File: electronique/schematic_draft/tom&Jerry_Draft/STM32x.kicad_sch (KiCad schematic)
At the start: 58 parts, among them IC4 STM32G431CBU3, J1 Conn_02x07_Odd_Even, SW1 SW_Push, SW2 SW_Push, SW3 SW_Push, SW4 SW_Push, Y1 16MHz

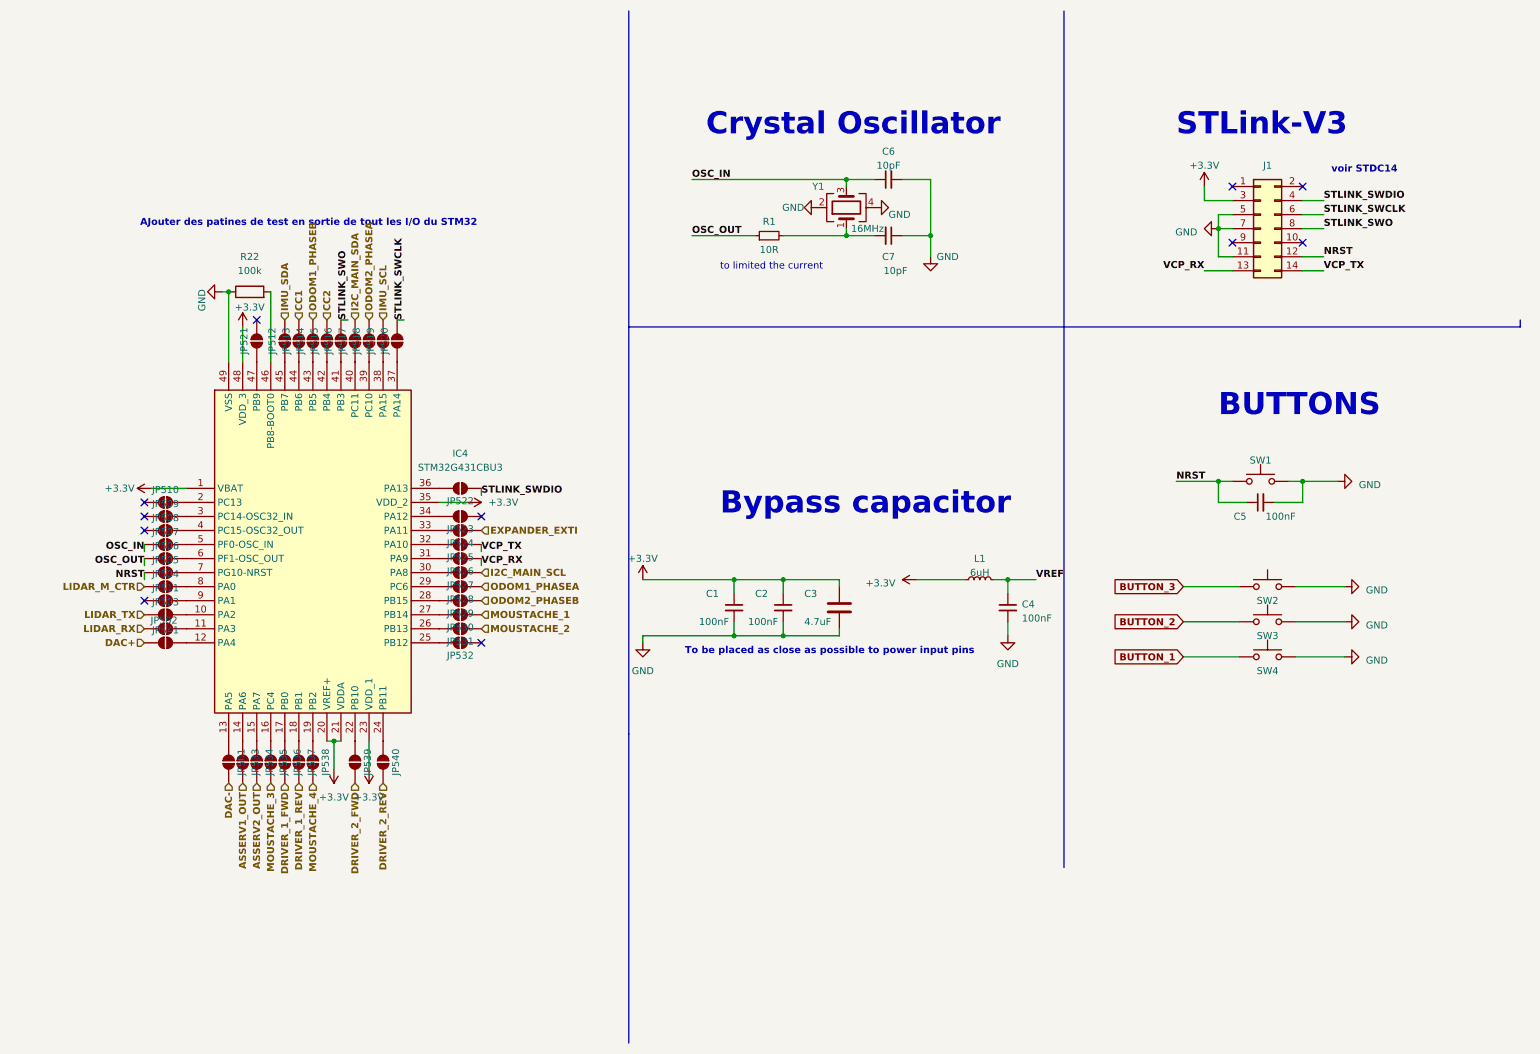
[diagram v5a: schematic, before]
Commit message: STM32 KiCAD V5 - 25.09.2024 - Ajout connecteurs TOF, ...
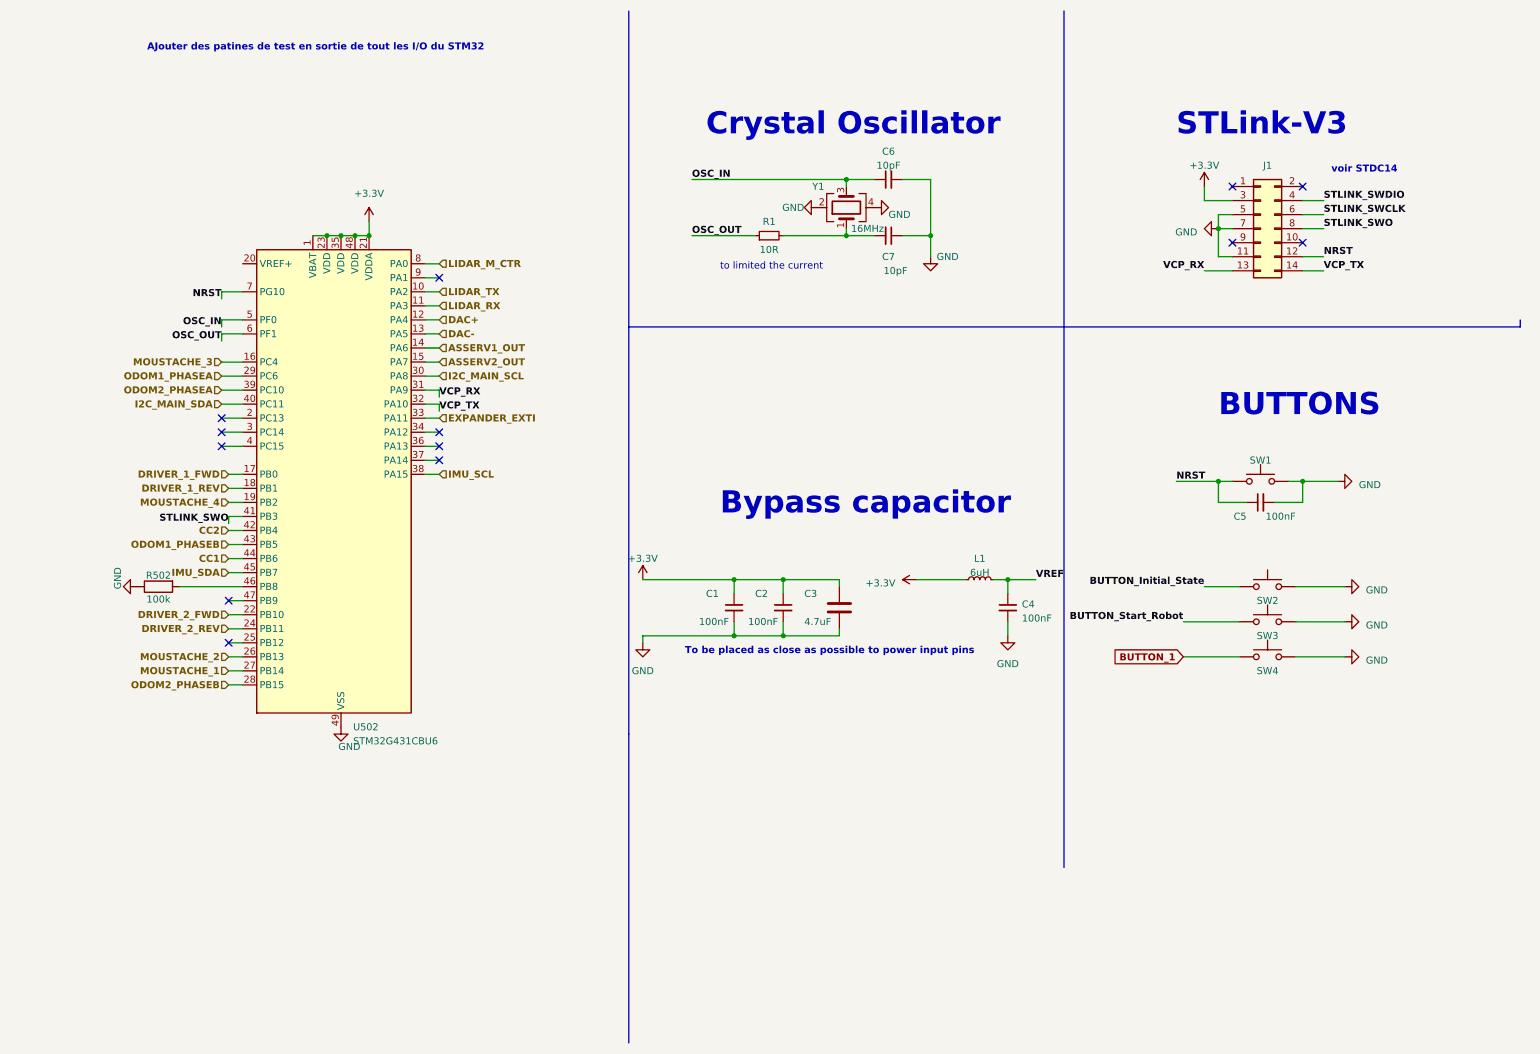
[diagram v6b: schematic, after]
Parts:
- removed IC4: STM32G431CBU3, QFN50P700X700X65-49N-D, symbol STM32G431CBU3:STM32G431CBU3
- removed JP501, JP502, JP503, JP504, JP505, JP506, JP507, JP508, JP509, JP510, JP511, JP512, JP513, JP514, JP515, JP516, JP517, JP518, JP519, JP520, JP521, JP522, JP523, JP524, JP525, JP526, JP527, JP528, JP529, JP530, JP531, JP532, JP533, JP534, JP535, JP536, JP537, JP538, JP539, JP540, JP541: SolderJumper_2_Open, symbol Jumper:SolderJumper_2_Open
- removed R22: 100k, symbol Device:R
- added R502: 100k, symbol Device:R
- added U502: STM32G431CBU6, Package_DFN_QFN:QFN-48-1EP_7x7mm_P0.5mm_EP5.6x5.6mm, symbol MCU_ST_STM32G4:STM32G431CBUx
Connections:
- net +3.3V: now also U502.1 (VBAT), U502.21 (VDDA), U502.23 (VDD), U502.35 (VDD), U502.48 (VDD)
- net ASSERV1_OUT: now also U502.14 (PA6)
- net ASSERV2_OUT: now also U502.15 (PA7)
- net CC1: now also U502.44 (PB6)
- net CC2: now also U502.42 (PB4)
- net DAC+: now also U502.12 (PA4)
- net DAC-: now also U502.13 (PA5)
- net DRIVER_1_FWD: now also U502.17 (PB0)
- net DRIVER_1_REV: now also U502.18 (PB1)
- net DRIVER_2_FWD: now also U502.22 (PB10)
- net DRIVER_2_REV: now also U502.24 (PB11)
- net EXPANDER_EXTI: now also U502.33 (PA11)
- net GND: now also R502.1, U502.49 (VSS)
- net I2C_MAIN_SCL: now also U502.30 (PA8)
- net I2C_MAIN_SDA: now also U502.40 (PC11)
- net IMU_SCL: now also U502.38 (PA15)
- net IMU_SDA: now also U502.45 (PB7)
- net LIDAR_M_CTR: now also U502.8 (PA0)
- net LIDAR_RX: now also U502.11 (PA3)
- net LIDAR_TX: now also U502.10 (PA2)
- net MOUSTACHE_1: now also U502.27 (PB14)
- net MOUSTACHE_2: now also U502.26 (PB13)
- net MOUSTACHE_3: now also U502.16 (PC4)
- net MOUSTACHE_4: now also U502.19 (PB2)
- net NRST: now also U502.7 (PG10)
- net ODOM1_PHASEA: now also U502.29 (PC6)
- net ODOM1_PHASEB: now also U502.43 (PB5)
- net ODOM2_PHASEA: now also U502.39 (PC10)
- net ODOM2_PHASEB: now also U502.28 (PB15)
- net OSC_IN: now also U502.5 (PF0)
- net OSC_OUT: now also U502.6 (PF1)
- net STLINK_SWO: now also U502.41 (PB3)
- net VCP_RX: now also U502.31 (PA9)
- net VCP_TX: now also U502.32 (PA10)
- net BUTTON_2 renamed BUTTON_Start_Robot
- net BUTTON_3 renamed BUTTON_Initial_State
- new net: R502.2, U502.46 (PB8)
- no-connect marks 11 -> 13

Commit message: STM32 KiCAD V6 - 25.09.2024 - Ajout des points test
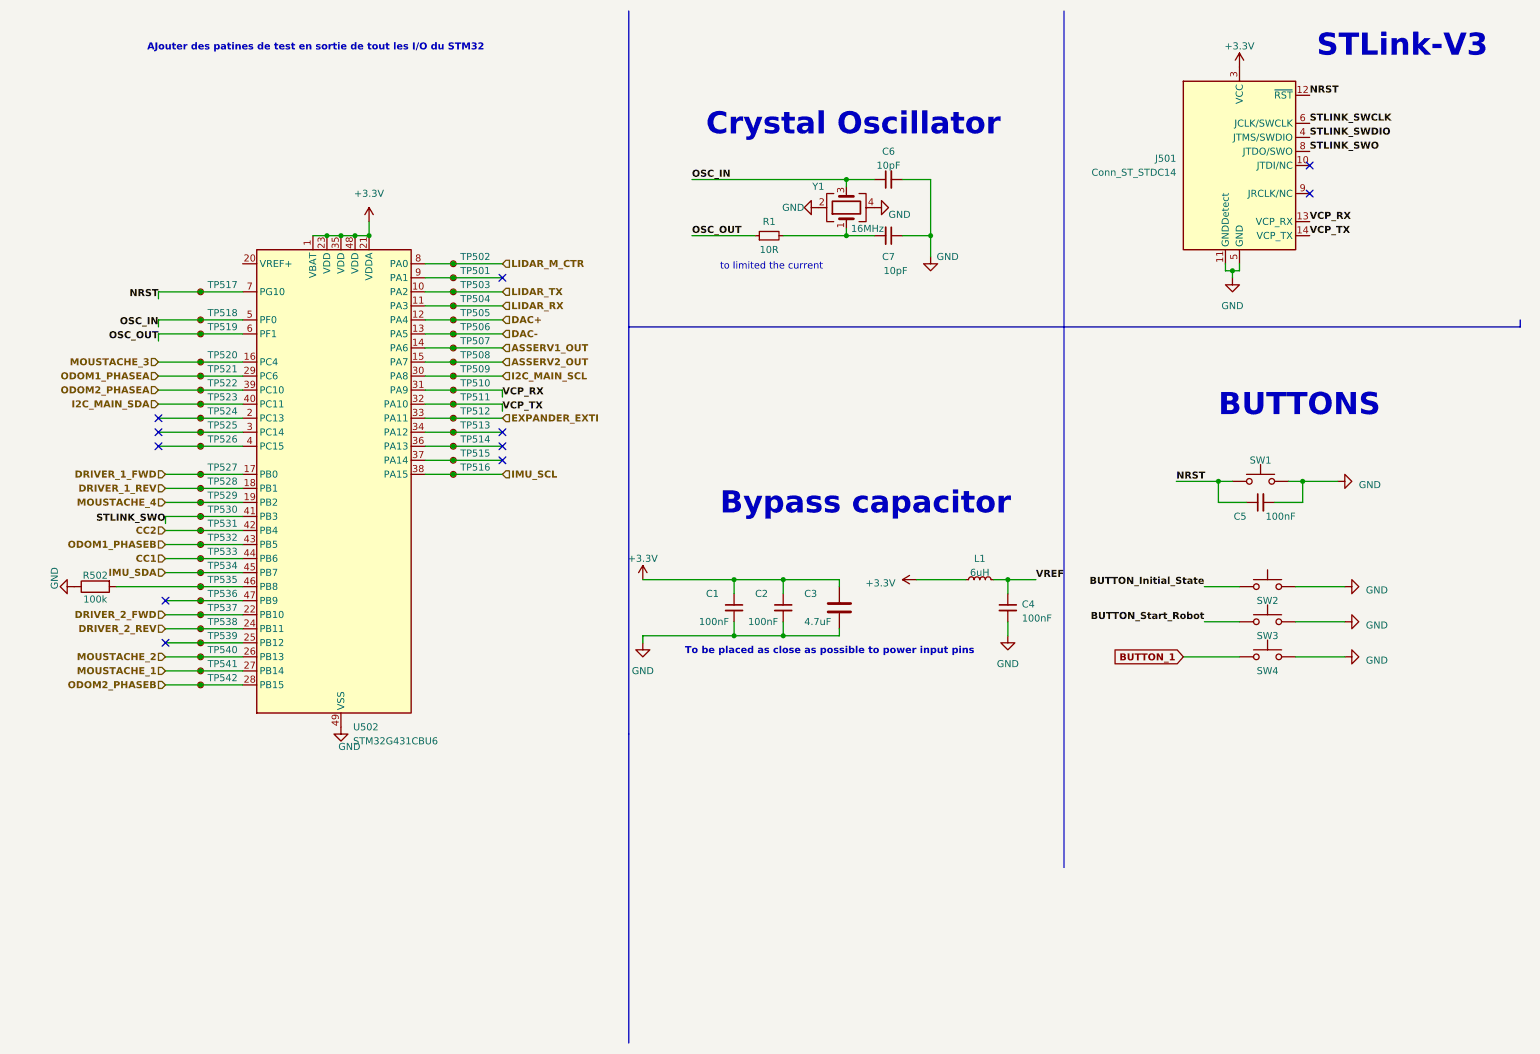
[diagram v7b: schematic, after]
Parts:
- removed J1: Conn_02x07_Odd_Even, Connector_PinHeader_1.27mm:PinHeader_2x07_P1.27mm_Vertical_SMD, symbol Connector_Generic:Conn_02x07_Odd_Even
- added J501: Conn_ST_STDC14, symbol Connector:Conn_ST_STDC14
- added TP501, TP502, TP503, TP504, TP505, TP506, TP507, TP508, TP509, TP510, TP511, TP512, TP513, TP514, TP515, TP516, TP517, TP518, TP519, TP520, TP521, TP522, TP523, TP524, TP525, TP526, TP527, TP528, TP529, TP530, TP531, TP532, TP533, TP534, TP535, TP536, TP537, TP538, TP539, TP540, TP541, TP542: TestPoint_Small, symbol Connector:TestPoint_Small
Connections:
- net +3.3V: now also J501.3 (VCC)
- net ASSERV1_OUT: now also TP507.1
- net ASSERV2_OUT: now also TP508.1
- net CC1: now also TP533.1
- net CC2: now also TP531.1
- net DAC+: now also TP505.1
- net DAC-: now also TP506.1
- net DRIVER_1_FWD: now also TP527.1
- net DRIVER_1_REV: now also TP528.1
- net DRIVER_2_FWD: now also TP537.1
- net DRIVER_2_REV: now also TP538.1
- net EXPANDER_EXTI: now also TP512.1
- net GND: now also J501.11 (GNDDetect), J501.5 (GND), J501.7 (GND)
- net I2C_MAIN_SCL: now also TP509.1
- net I2C_MAIN_SDA: now also TP523.1
- net IMU_SCL: now also TP516.1
- net IMU_SDA: now also TP534.1
- net LIDAR_M_CTR: now also TP502.1
- net LIDAR_RX: now also TP504.1
- net LIDAR_TX: now also TP503.1
- net MOUSTACHE_1: now also TP541.1
- net MOUSTACHE_2: now also TP540.1
- net MOUSTACHE_3: now also TP520.1
- net MOUSTACHE_4: now also TP529.1
- net NRST: now also J501.12 (~{RST}), TP517.1
- net ODOM1_PHASEA: now also TP521.1
- net ODOM1_PHASEB: now also TP532.1
- net ODOM2_PHASEA: now also TP522.1
- net ODOM2_PHASEB: now also TP542.1
- net OSC_IN: now also TP518.1
- net OSC_OUT: now also TP519.1
- net STLINK_SWCLK: now also J501.6 (JCLK/SWCLK)
- net STLINK_SWDIO: now also J501.4 (JTMS/SWDIO)
- net STLINK_SWO: now also J501.8 (JTDO/SWO), TP530.1
- net VCP_RX: now also J501.13 (VCP_RX), TP510.1
- net VCP_TX: now also J501.14 (VCP_TX), TP511.1
- net at R502.2, U502.46 (PB8): now also TP535.1
- net at U502.2 (PC13): now also TP524.1
- net at U502.25 (PB12): now also TP539.1
- net at U502.3 (PC14): now also TP525.1
- net at U502.34 (PA12): now also TP513.1
- net at U502.36 (PA13): now also TP514.1
- net at U502.37 (PA14): now also TP515.1
- net at U502.4 (PC15): now also TP526.1
- net at U502.47 (PB9): now also TP536.1
- net at U502.9 (PA1): now also TP501.1
- no-connect marks 13 -> 11
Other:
- note removed: "voir STDC14"
- moved on the sheet: R502

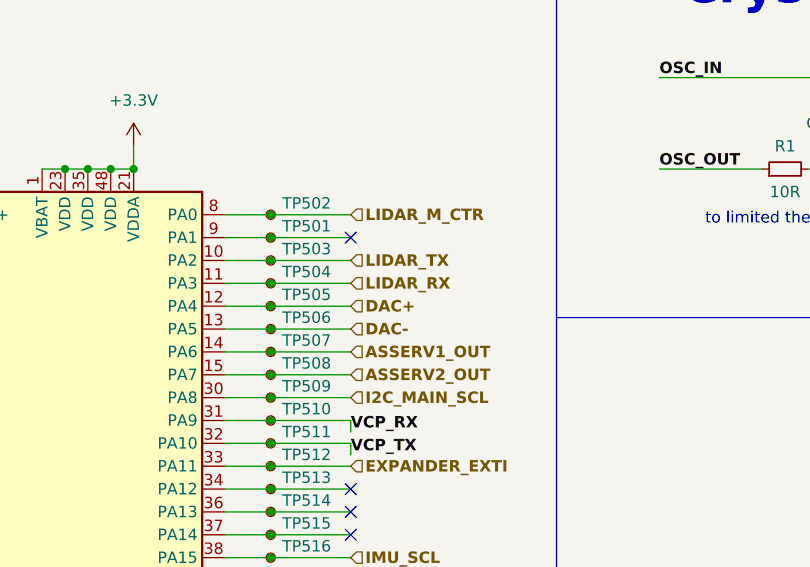
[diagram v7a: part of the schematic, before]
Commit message: STM32 KiCAD V6 - 25.09.2024 - Nettoyage des mauvais pins
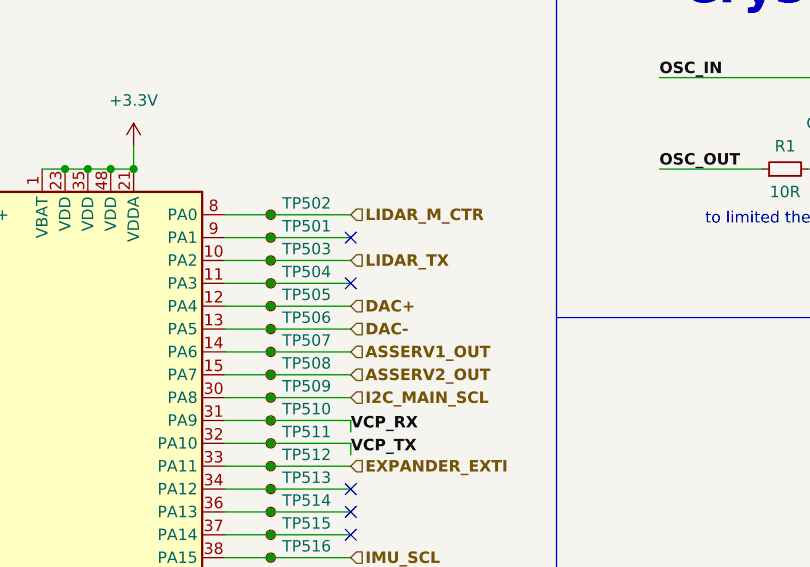
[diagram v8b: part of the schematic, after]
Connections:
- net LIDAR_RX: no longer names the net of TP504.1, U502.11 (PA3)
- no-connect marks 11 -> 12
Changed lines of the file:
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@@
+	)
+	(no_connect
+		(at 101.6 64.77)
 	)
 	(no_connect
@@
 		(fields_autoplaced yes)
 		(effects
-			(font
-				(size 1.27 1.27)
-				(thickness 0.254)
-				(bold yes)
-			)
-			(justify left)
-		)
-	)
-	(hierarchical_label "LIDAR_RX"
-		(shape input)
-		(at 101.6 64.77 0)
-		(fields_autoplaced yes)
-		(effects
